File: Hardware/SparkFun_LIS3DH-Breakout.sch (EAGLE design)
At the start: 18 parts, among them U2 LIS3DH

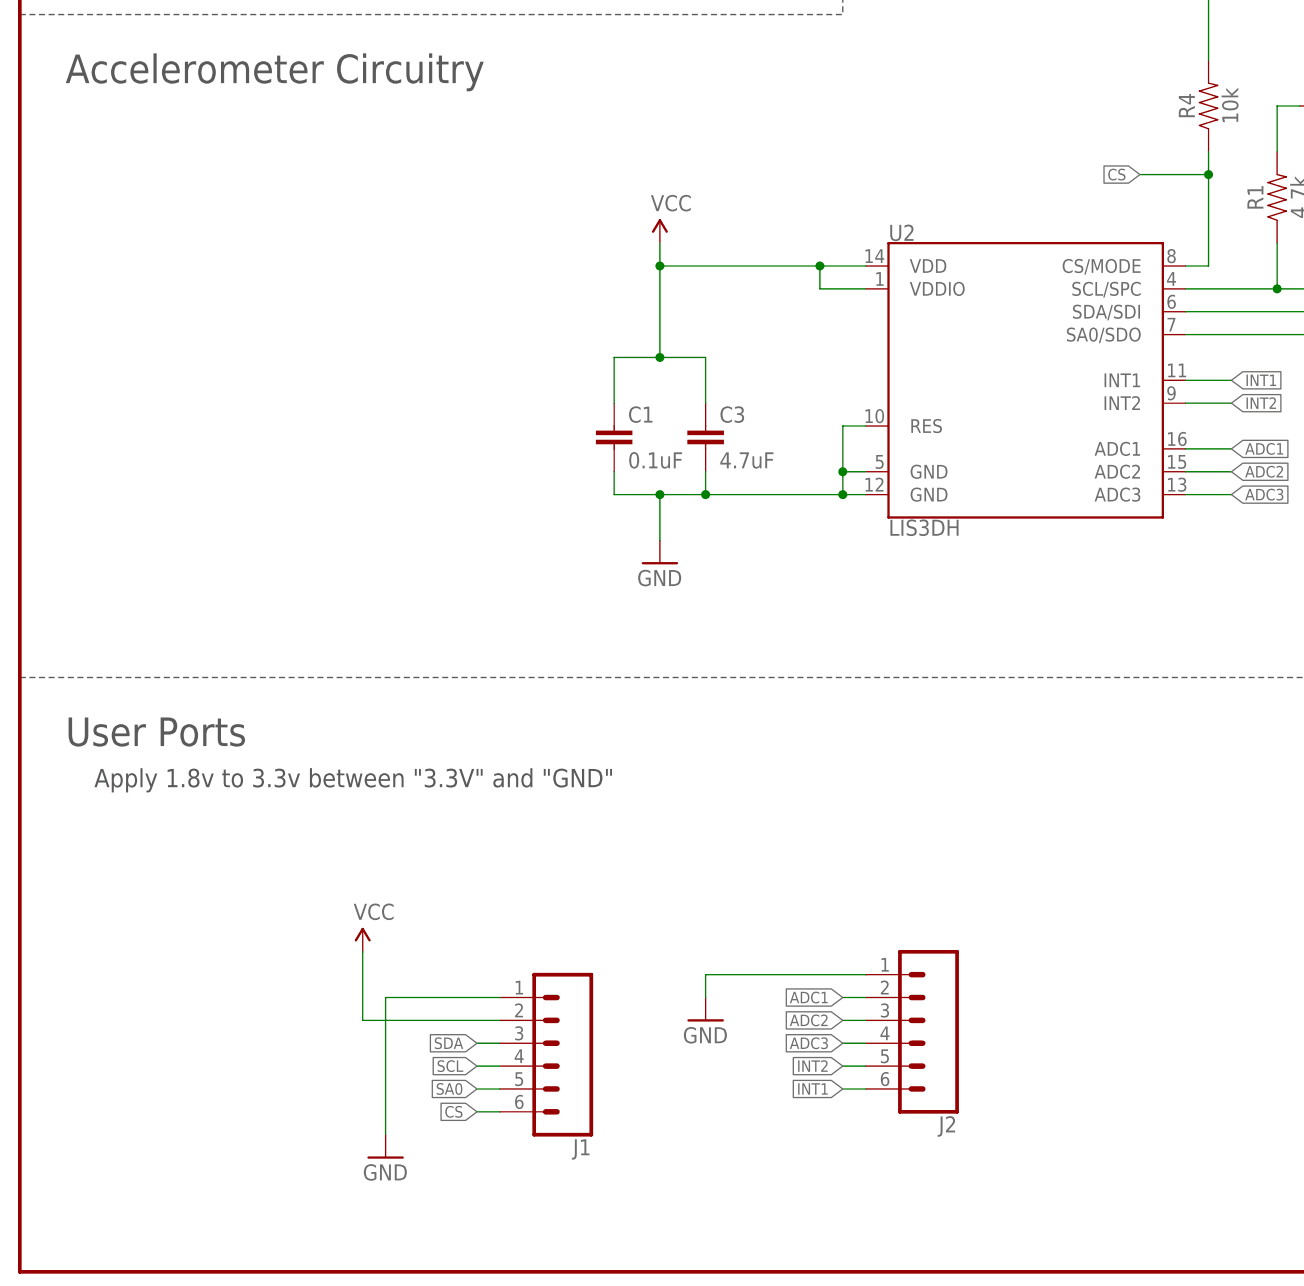
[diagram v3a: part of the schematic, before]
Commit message: Adjusted a trace and updated components to most recent libraries
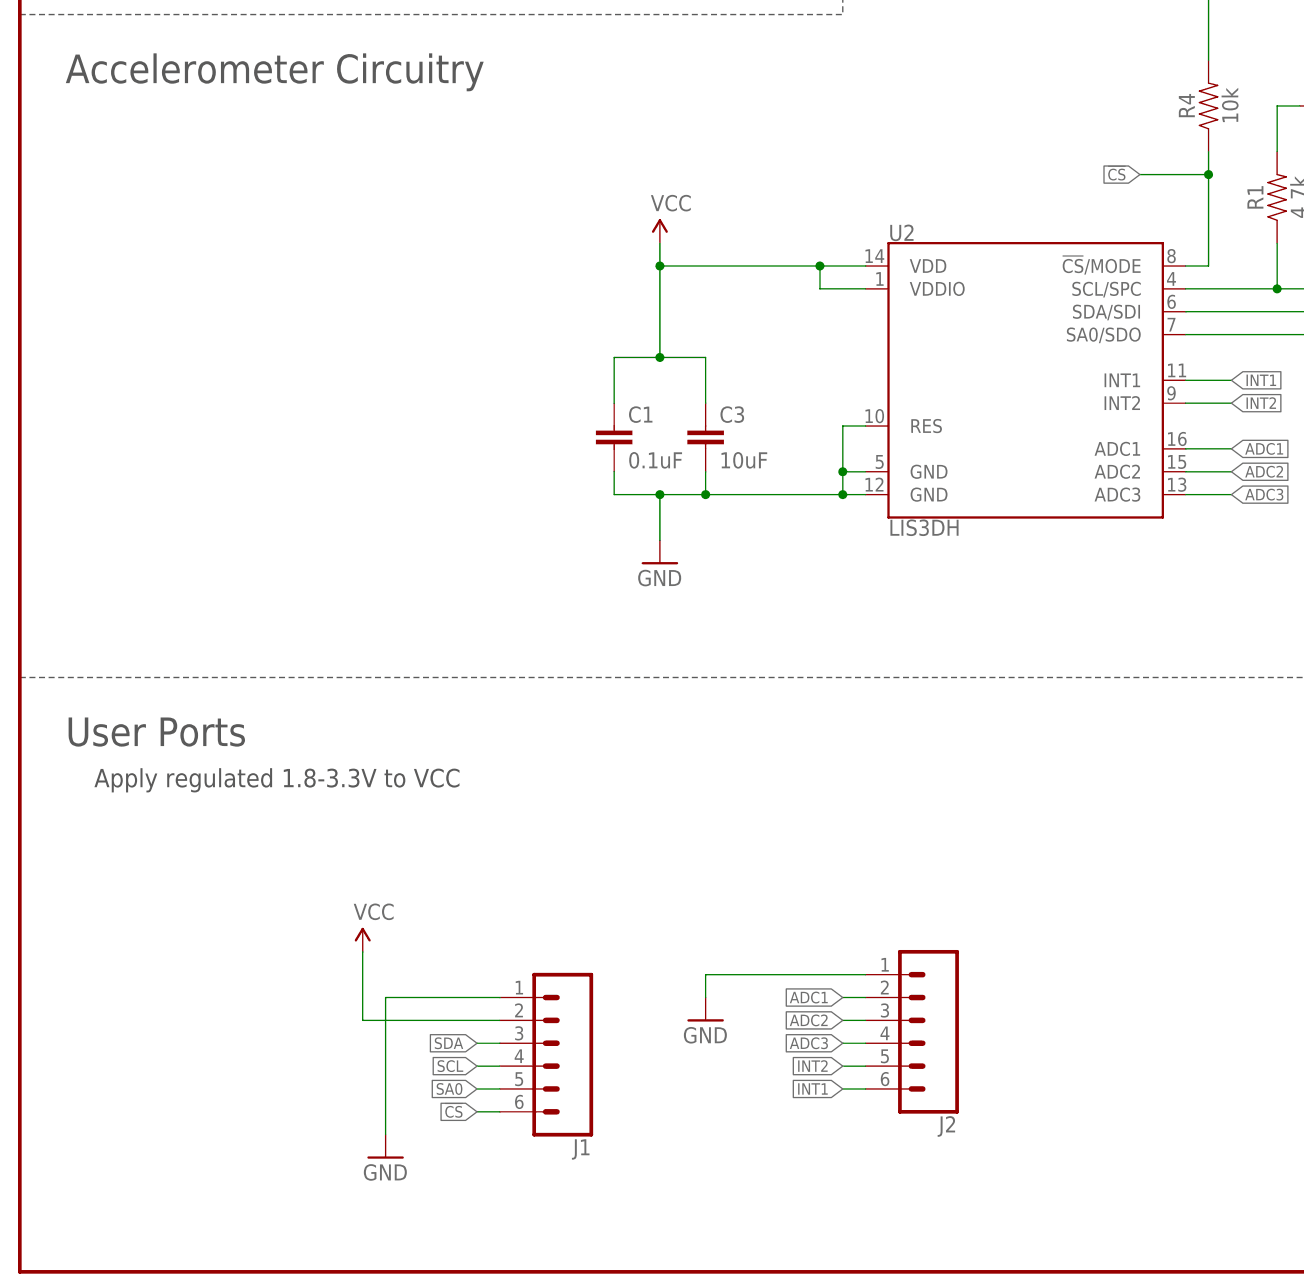
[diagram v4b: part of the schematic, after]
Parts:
- C1: device SparkFun:CAP0402-CAP -> SparkFun-Capacitors:0.1UF-0402-16V-10%
- C3: value 4.7uF -> 10uF; device SparkFun:CAP0402-CAP -> SparkFun-Capacitors:10UF-0603-6.3V-20%
- J1, J2: device SparkFun-Connectors:CONN_06SILK_FEMALE_PTH -> SparkFun-Connectors:CONN_06NO_SILK_FEMALE_PTH
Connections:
- removed net 3.3V: C1.1, C3.1, R3.2, R4.2, SJ2.2, U2.VDD, U2.VDDIO
- removed net CS: J1.6, R4.1, U2.CS/MODE
- new net !CS: J1.6, R4.1, U2.!CS!/MODE
- net VCC: now also C1.1, C3.1, R3.2, R4.2, SJ2.2, U2.VDD, U2.VDDIO
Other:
- note added: "Apply regulated 1.8-3.3V to VCC"
- note removed: "Apply 1.8v to 3.3v between "3.3V" and "GND""
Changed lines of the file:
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@@
 </classes>
 <parts>
-<part name="C1" library="SparkFun" deviceset="CAP" device="0402-CAP" value="0.1uF"/>
-<part name="C3" library="SparkFun" deviceset="CAP" device="0402-CAP" value="4.7uF"/>
+<part name="C1" library="SparkFun-Capacitors" deviceset="0.1UF" device="-0402-16V-10%" value="0.1uF"/>
+<part name="C3" library="SparkFun-Capacitors" deviceset="10UF" device="-0603-6.3V-20%" value="10uF"/>
 <part name="R1" library="SparkFun-Resistors" deviceset="4.7KOHM" device="-0603-1/10W-1%" value="4.7k"/>
 <part name="R2" library="SparkFun-Resistors" deviceset="4.7KOHM" device="-0603-1/10W-1%" value="4.7k"/>
@@
 <part name="SJ2" library="TestAperatures" deviceset="JUMPER-PAD-3-NC_BY_TRACE" device=""/>
 <part name="R4" library="SparkFun-Resistors" deviceset="10KOHM" device="-0603-1/10W-1%" value="10k"/>
-<part name="J1" library="SparkFun-Connectors" deviceset="CONN_06" device="SILK_FEMALE_PTH"/>
+<part name="J1" library="SparkFun-Connectors" deviceset="CONN_06" device="NO_SILK_FEMALE_PTH"/>
 <part name="FRAME2" library="SparkFun-Aesthetics" deviceset="FRAME-LETTER" device=""/>
 <part name="LOGO1" library="SparkFun-Aesthetics" deviceset="SFE_LOGO_FLAME" device=".1_INCH"/>
 <part name="SUPPLY1" library="SparkFun-Aesthetics" deviceset="VCC" device=""/>
 <part name="GND3" library="SparkFun" deviceset="GND" device=""/>
-<part name="J2" library="SparkFun-Connectors" deviceset="CONN_06" device="SILK_FEMALE_PTH"/>
+<part name="J2" library="SparkFun-Connectors" deviceset="CONN_06" device="NO_SILK_FEMALE_PTH"/>
 <part name="GND4" library="SparkFun" deviceset="GND" device=""/>
 </parts>
@@
 <text x="5.08" y="132.08" size="3.175" layer="97">Accelerometer Circuitry</text>
 <text x="5.08" y="58.42" size="3.175" layer="97">User Ports</text>
-<text x="5.08" y="55.88" size="2.032" layer="97" align="top-left">    Apply 1.8v to 3.3v between "3.3V" and "GND"</text>
+<text x="5.08" y="55.88" size="2.032" layer="97" align="top-left">    Apply regulated 1.8-3.3V to VCC</text>
 <wire x1="147.32" y1="66.04" x2="248.92" y2="66.04" width="0.1524" layer="97" style="longdash"/>
 <wire x1="0" y1="139.7" x2="91.44" y2="139.7" width="0.1524" layer="97" style="longdash"/>
@@
 </busses>
 <nets>
-<net name="3.3V" class="0">
-<segment>
-<wire x1="71.12" y1="101.6" x2="71.12" y2="111.76" width="0.1524" layer="91"/>
-<wire x1="71.12" y1="111.76" x2="71.12" y2="114.3" width="0.1524" layer="91"/>
-<wire x1="76.2" y1="96.52" x2="76.2" y2="101.6" width="0.1524" layer="91"/>
-<wire x1="76.2" y1="101.6" x2="71.12" y2="101.6" width="0.1524" layer="91"/>
-<wire x1="66.04" y1="96.52" x2="66.04" y2="101.6" width="0.1524" layer="91"/>
-<wire x1="66.04" y1="101.6" x2="71.12" y2="101.6" width="0.1524" layer="91"/>
-<pinref part="P+1" gate="G$1" pin="VCC"/>
-<pinref part="C3" gate="G$1" pin="1"/>
-<pinref part="C1" gate="G$1" pin="1"/>
-<wire x1="71.12" y1="111.76" x2="88.9" y2="111.76" width="0.1524" layer="91"/>
-<wire x1="88.9" y1="111.76" x2="88.9" y2="109.22" width="0.1524" layer="91"/>
-<pinref part="U2" gate="G$1" pin="VDDIO"/>
-<wire x1="88.9" y1="109.22" x2="93.98" y2="109.22" width="0.1524" layer="91"/>
-<pinref part="U2" gate="G$1" pin="VDD"/>
-<wire x1="88.9" y1="111.76" x2="93.98" y2="111.76" width="0.1524" layer="91"/>
-<junction x="88.9" y="111.76"/>
-<junction x="71.12" y="111.76"/>
-<junction x="71.12" y="101.6"/>
-</segment>
-<segment>
-<wire x1="172.72" y1="119.38" x2="172.72" y2="116.84" width="0.1524" layer="91"/>
-<pinref part="R3" gate="G$1" pin="2"/>
-<pinref part="P+4" gate="G$1" pin="VCC"/>
-</segment>
-<segment>
-<pinref part="P+3" gate="G$1" pin="VCC"/>
-<pinref part="SJ2" gate="G$1" pin="2"/>
-<wire x1="147.32" y1="144.78" x2="147.32" y2="134.62" width="0.1524" layer="91"/>
-</segment>
-<segment>
-<pinref part="R4" gate="G$1" pin="2"/>
-<pinref part="P+2" gate="G$1" pin="VCC"/>
-<wire x1="132.08" y1="134.62" x2="132.08" y2="144.78" width="0.1524" layer="91"/>
-</segment>
-</net>
 <net name="GND" class="0">
 <segment>
@@
 </segment>
 </net>
-<net name="CS" class="0">
-<segment>
-<pinref part="U2" gate="G$1" pin="CS/MODE"/>
+<net name="!CS" class="0">
+<segment>
+<pinref part="U2" gate="G$1" pin="!CS!/MODE"/>
 <wire x1="129.54" y1="111.76" x2="132.08" y2="111.76" width="0.1524" layer="91"/>
 <pinref part="R4" gate="G$1" pin="1"/>
@@
 <wire x1="38.1" y1="27.94" x2="38.1" y2="35.56" width="0.1524" layer="91"/>
 </segment>
-</net>
+<segment>
+<pinref part="R4" gate="G$1" pin="2"/>
+<pinref part="P+2" gate="G$1" pin="VCC"/>
+<wire x1="132.08" y1="134.62" x2="132.08" y2="144.78" width="0.1524" layer="91"/>
+</segment>
+<segment>
+<pinref part="P+3" gate="G$1" pin="VCC"/>
+<pinref part="SJ2" gate="G$1" pin="2"/>
+<wire x1="147.32" y1="144.78" x2="147.32" y2="134.62" width="0.1524" layer="91"/>
+</segment>
+<segment>
+<wire x1="172.72" y1="119.38" x2="172.72" y2="116.84" width="0.1524" layer="91"/>
+<pinref part="R3" gate="G$1" pin="2"/>
+<pinref part="P+4" gate="G$1" pin="VCC"/>
+</segment>
+<segment>
+<wire x1="71.12" y1="101.6" x2="71.12" y2="111.76" width="0.1524" layer="91"/>
+<wire x1="71.12" y1="111.76" x2="71.12" y2="114.3" width="0.1524" layer="91"/>
+<wire x1="76.2" y1="96.52" x2="76.2" y2="101.6" width="0.1524" layer="91"/>
+<wire x1="76.2" y1="101.6" x2="71.12" y2="101.6" width="0.1524" layer="91"/>
+<wire x1="66.04" y1="96.52" x2="66.04" y2="101.6" width="0.1524" layer="91"/>
+<wire x1="66.04" y1="101.6" x2="71.12" y2="101.6" width="0.1524" layer="91"/>
+<pinref part="P+1" gate="G$1" pin="VCC"/>
+<pinref part="C3" gate="G$1" pin="1"/>
+<pinref part="C1" gate="G$1" pin="1"/>
+<wire x1="71.12" y1="111.76" x2="88.9" y2="111.76" width="0.1524" layer="91"/>
+<wire x1="88.9" y1="111.76" x2="88.9" y2="109.22" width="0.1524" layer="91"/>
+<pinref part="U2" gate="G$1" pin="VDDIO"/>
+<wire x1="88.9" y1="109.22" x2="93.98" y2="109.22" width="0.1524" layer="91"/>
+<pinref part="U2" gate="G$1" pin="VDD"/>
+<wire x1="88.9" y1="111.76" x2="93.98" y2="111.76" width="0.1524" layer="91"/>
+<junction x="88.9" y="111.76"/>
+<junction x="71.12" y="111.76"/>
+<junction x="71.12" y="101.6"/>
+</segment>
+</net>

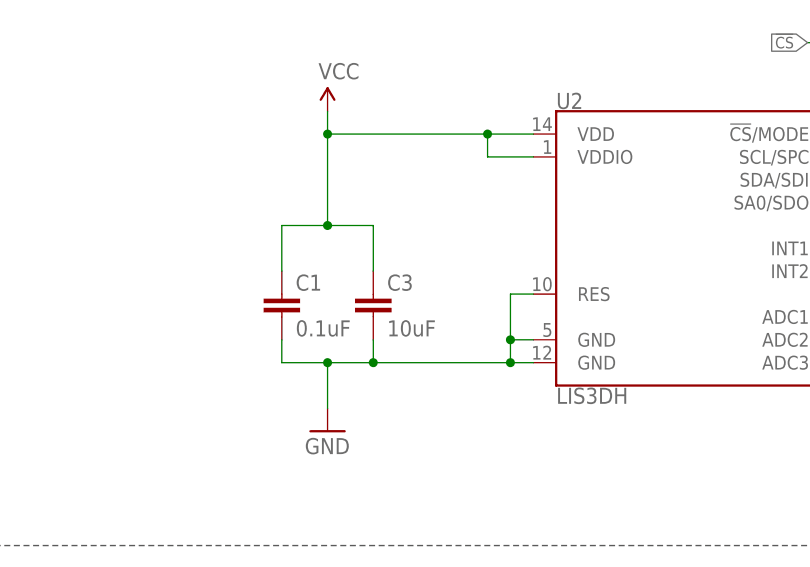
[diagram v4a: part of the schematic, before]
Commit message: fixed airwire and renamed C3 to C2
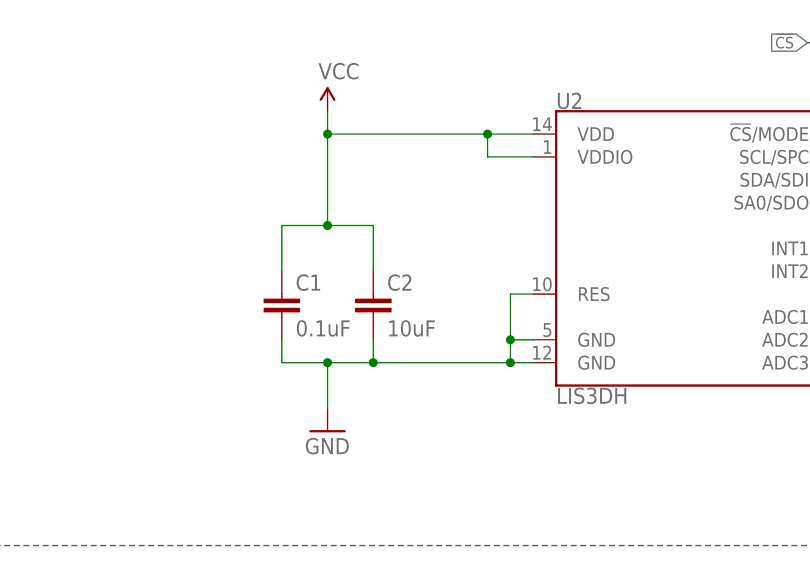
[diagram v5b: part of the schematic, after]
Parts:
- renumbered C3 to C2
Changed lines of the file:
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@@
 <parts>
 <part name="C1" library="SparkFun-Capacitors" deviceset="0.1UF" device="-0402-16V-10%" value="0.1uF"/>
-<part name="C3" library="SparkFun-Capacitors" deviceset="10UF" device="-0603-6.3V-20%" value="10uF"/>
+<part name="C2" library="SparkFun-Capacitors" deviceset="10UF" device="-0603-6.3V-20%" value="10uF"/>
 <part name="R1" library="SparkFun-Resistors" deviceset="4.7KOHM" device="-0603-1/10W-1%" value="4.7k"/>
 <part name="R2" library="SparkFun-Resistors" deviceset="4.7KOHM" device="-0603-1/10W-1%" value="4.7k"/>
@@
 <instances>
 <instance part="C1" gate="G$1" x="66.04" y="91.44"/>
-<instance part="C3" gate="G$1" x="76.2" y="91.44"/>
+<instance part="C2" gate="G$1" x="76.2" y="91.44"/>
 <instance part="R1" gate="G$1" x="139.7" y="119.38" rot="R90"/>
 <instance part="R2" gate="G$1" x="154.94" y="116.84" rot="R90"/>
@@
 <pinref part="GND1" gate="1" pin="GND"/>
 <pinref part="C1" gate="G$1" pin="2"/>
-<pinref part="C3" gate="G$1" pin="2"/>
+<pinref part="C2" gate="G$1" pin="2"/>
 <pinref part="U2" gate="G$1" pin="GND@12"/>
 <wire x1="91.44" y1="86.36" x2="93.98" y2="86.36" width="0.1524" layer="91"/>
@@
 <wire x1="66.04" y1="101.6" x2="71.12" y2="101.6" width="0.1524" layer="91"/>
 <pinref part="P+1" gate="G$1" pin="VCC"/>
-<pinref part="C3" gate="G$1" pin="1"/>
+<pinref part="C2" gate="G$1" pin="1"/>
 <pinref part="C1" gate="G$1" pin="1"/>
 <wire x1="71.12" y1="111.76" x2="88.9" y2="111.76" width="0.1524" layer="91"/>

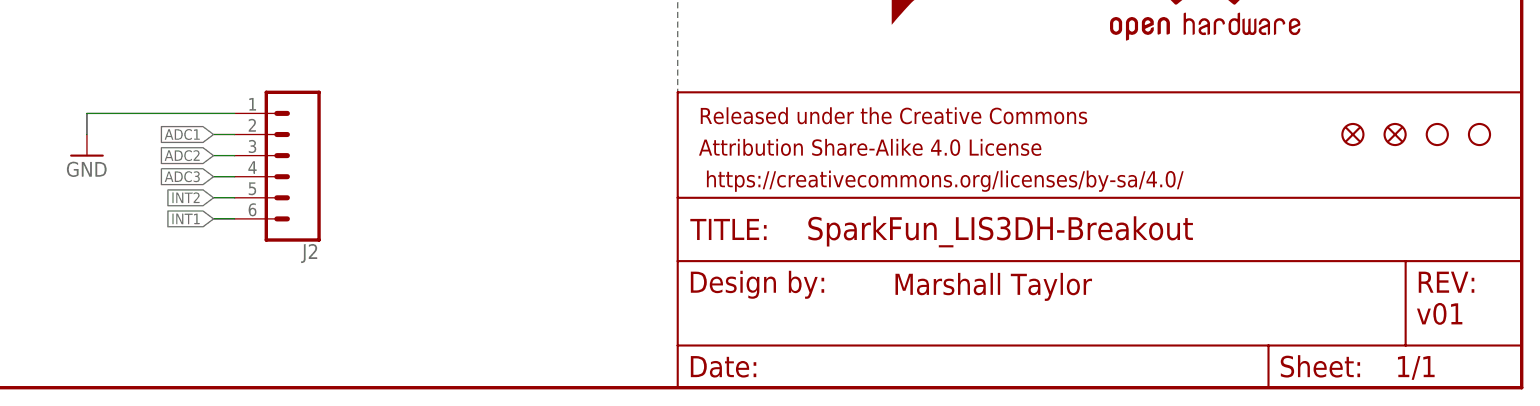
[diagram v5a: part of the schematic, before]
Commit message: Fixed silk: added address/jumper function, pumped up the product name silk.  Swapped I1 and I2.  Added more topside labeling
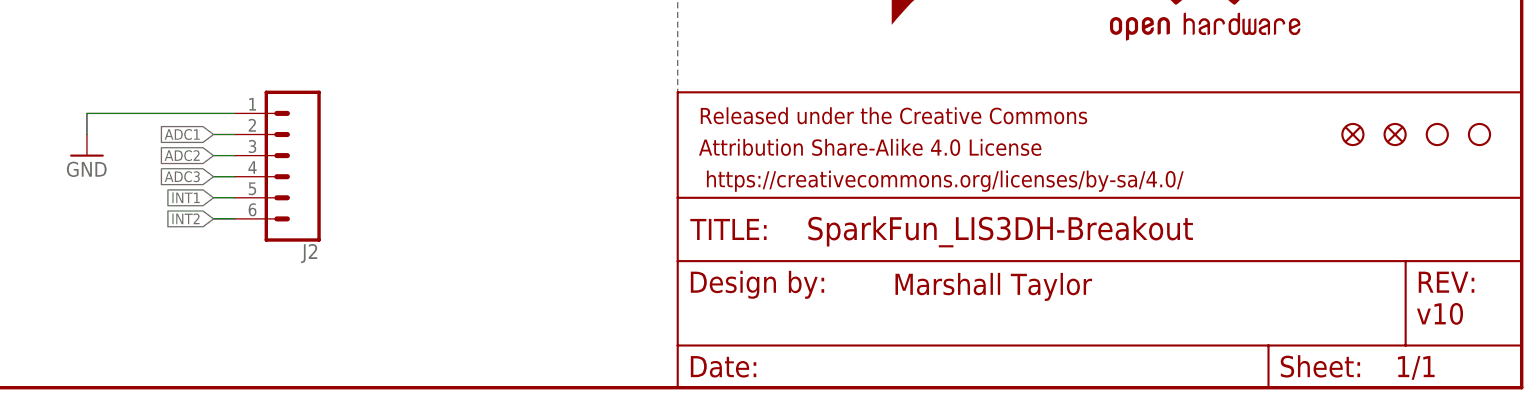
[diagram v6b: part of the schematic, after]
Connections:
- net INT1: now also J2.5; no longer J2.6
- net INT2: now also J2.6; no longer J2.5
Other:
- note added: "v10"
- note removed: "v01"
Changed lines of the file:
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@@
 <text x="182.88" y="86.36" size="1.778" layer="97">SA0 = 1: 0x19</text>
 <text x="177.8" y="96.52" size="1.778" layer="97">Jumper open by default, so SA0 = 1</text>
-<text x="236.22" y="7.62" size="2.54" layer="94">v01</text>
+<text x="236.22" y="7.62" size="2.54" layer="94">v10</text>
 <text x="173.228" y="11.176" size="2.54" layer="94">Marshall Taylor</text>
 <text x="5.08" y="177.8" size="3.81" layer="97">LIS3DH Breakout</text>
@@
 </segment>
 <segment>
+<wire x1="93.98" y1="20.32" x2="91.44" y2="20.32" width="0.1524" layer="91"/>
+<label x="91.44" y="20.32" size="1.27" layer="95" rot="R180" xref="yes"/>
+<pinref part="J2" gate="G$1" pin="6"/>
+</segment>
+</net>
+<net name="INT1" class="0">
+<segment>
+<wire x1="129.54" y1="99.06" x2="134.62" y2="99.06" width="0.1524" layer="91"/>
+<pinref part="U2" gate="G$1" pin="INT1"/>
+<label x="134.62" y="99.06" size="1.27" layer="95" font="vector" xref="yes"/>
+</segment>
+<segment>
 <wire x1="93.98" y1="22.86" x2="91.44" y2="22.86" width="0.1524" layer="91"/>
 <label x="91.44" y="22.86" size="1.27" layer="95" rot="R180" xref="yes"/>
 <pinref part="J2" gate="G$1" pin="5"/>
-</segment>
-</net>
-<net name="INT1" class="0">
-<segment>
-<wire x1="93.98" y1="20.32" x2="91.44" y2="20.32" width="0.1524" layer="91"/>
-<label x="91.44" y="20.32" size="1.27" layer="95" rot="R180" xref="yes"/>
-<pinref part="J2" gate="G$1" pin="6"/>
-</segment>
-<segment>
-<wire x1="129.54" y1="99.06" x2="134.62" y2="99.06" width="0.1524" layer="91"/>
-<pinref part="U2" gate="G$1" pin="INT1"/>
-<label x="134.62" y="99.06" size="1.27" layer="95" font="vector" xref="yes"/>
 </segment>
 </net>
@@
 </sheet>
 </sheets>
+<errors>
+</errors>
 </schematic>
 </drawing>
